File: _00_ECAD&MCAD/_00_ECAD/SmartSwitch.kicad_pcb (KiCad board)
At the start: 2 copper layers, 87 x 63 mm, 61 parts, among them J1 SWITCH, K1 G5LE-1, K2 G5LE-1, Q1 MMBT5550L, Q2 MMBT5550L, Q3 MMBT5550L, Q4 MMBT5550L, U1 DS1822, U2 ESP-12F, U3 MCP1825S

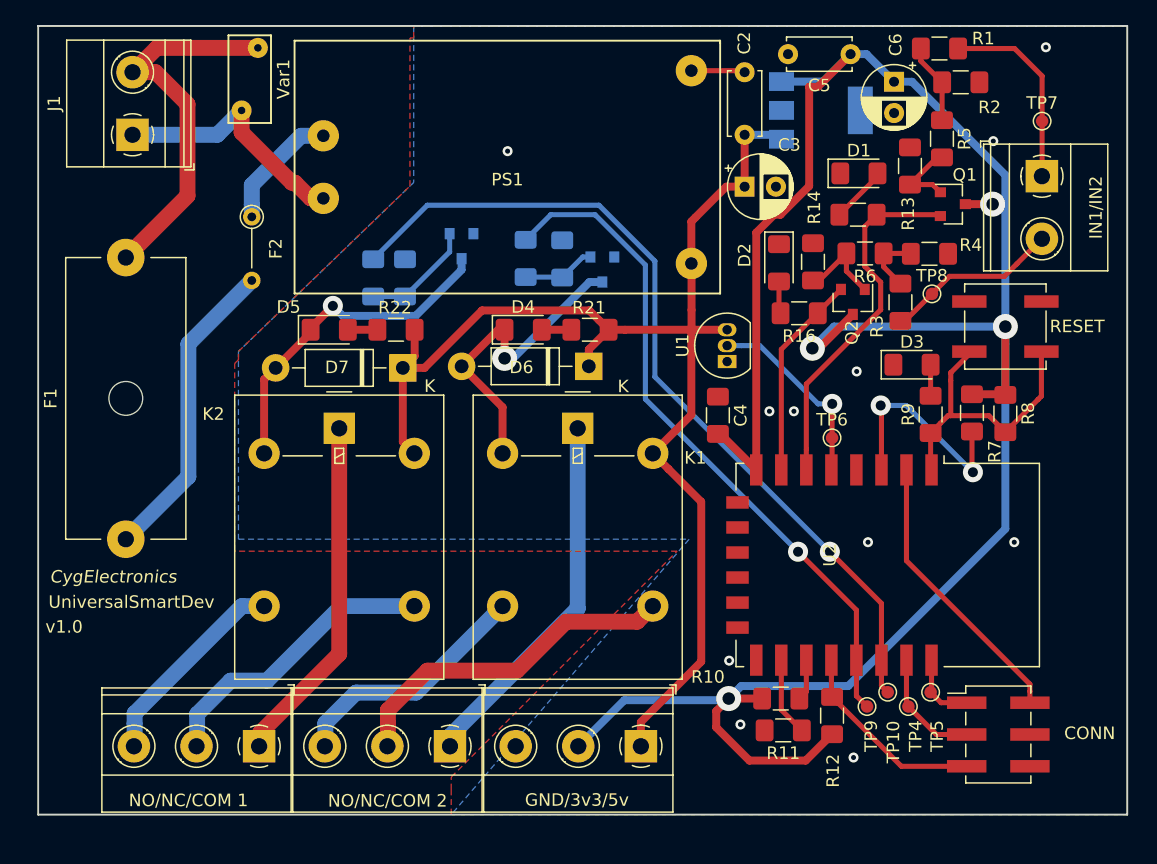
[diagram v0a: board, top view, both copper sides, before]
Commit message: Fix LED, common emitter issue, add adc feature
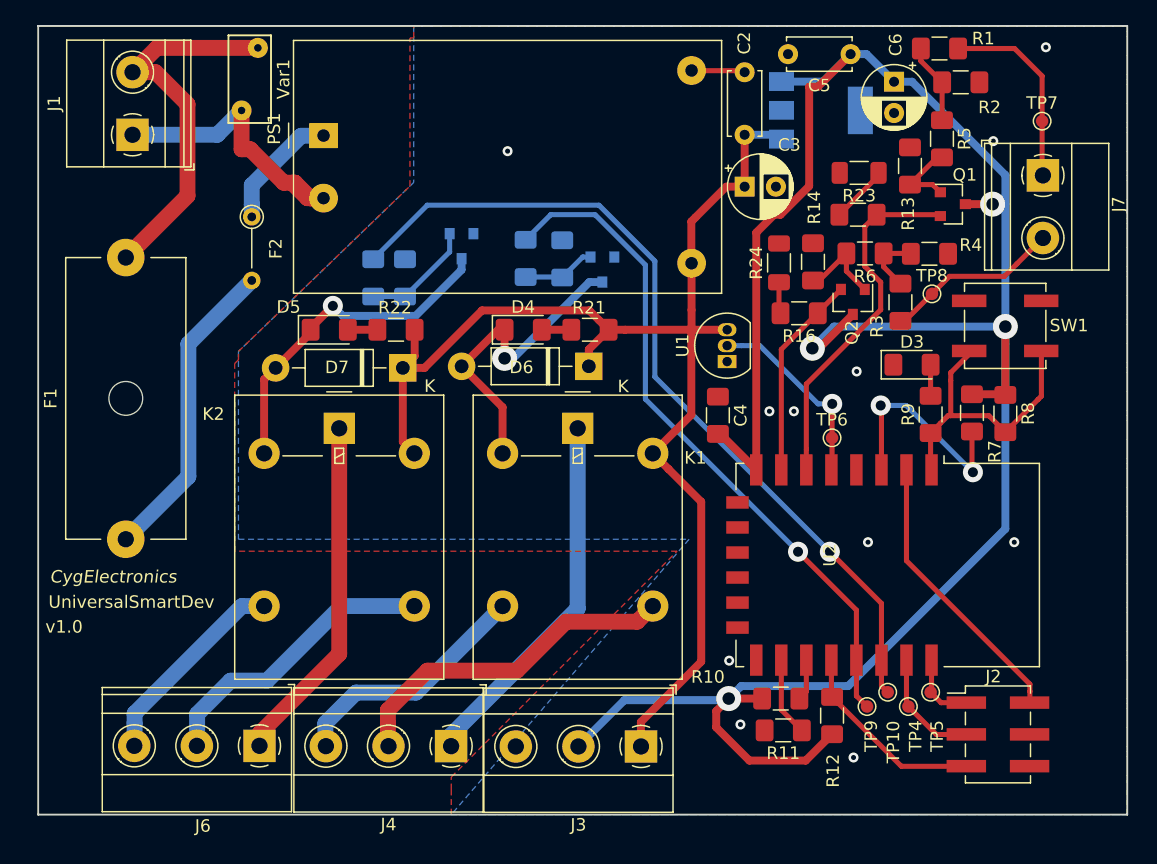
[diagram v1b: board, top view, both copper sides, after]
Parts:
- removed CONN: Conn_02x03_Counter_Clockwise, Connector_PinHeader_2.54mm:PinHeader_2x03_P2.54mm_Vertical_SMD
- removed D1, D2: LED, LED_SMD:LED_1206_3216Metric_Pad1.42x1.75mm_HandSolder
- removed GND/3v3/5v: Screw_Terminal_01x03, TerminalBlock_Phoenix:TerminalBlock_Phoenix_MKDS-1,5-3_1x03_P5.00mm_Horizontal
- removed IN1/IN2: INPUT, TerminalBlock_Phoenix:TerminalBlock_Phoenix_MKDS-1,5-2_1x02_P5.00mm_Horizontal
- removed NO/NC/COM 1: Screw_Terminal_01x03, TerminalBlock_Phoenix:TerminalBlock_Phoenix_MKDS-1,5-3_1x03_P5.00mm_Horizontal
- removed NO/NC/COM 2: Screw_Terminal_01x03, TerminalBlock_Phoenix:TerminalBlock_Phoenix_MKDS-1,5-3_1x03_P5.00mm_Horizontal
- removed RESET: RESET, Button_Switch_SMD:SW_SPST_B3SL-1022P
- added J2: Conn_02x03_Counter_Clockwise, Connector_PinHeader_2.54mm:PinHeader_2x03_P2.54mm_Vertical_SMD, F.Cu at (171.7, 141.6)
- added J3: Screw_Terminal_01x03, TerminalBlock_Phoenix:TerminalBlock_Phoenix_MKDS-1,5-3_1x03_P5.00mm_Horizontal, F.Cu at (143.2, 142.6)
- added J4: Screw_Terminal_01x03, TerminalBlock_Phoenix:TerminalBlock_Phoenix_MKDS-1,5-3_1x03_P5.00mm_Horizontal, F.Cu at (128.0, 142.5)
- added J6: Screw_Terminal_01x03, TerminalBlock_Phoenix:TerminalBlock_Phoenix_MKDS-1,5-3_1x03_P5.00mm_Horizontal, F.Cu at (112.7, 142.5)
- added J7: INPUT, TerminalBlock_Phoenix:TerminalBlock_Phoenix_MKDS-1,5-2_1x02_P5.00mm_Horizontal, F.Cu at (175.3, 96.9)
- added R23: 10k, Resistor_SMD:R_1206_3216Metric_Pad1.30x1.75mm_HandSolder, F.Cu at (160.6, 96.7)
- added R24: 10k, Resistor_SMD:R_1206_3216Metric_Pad1.30x1.75mm_HandSolder, F.Cu at (154.2, 103.9)
- added SW1: RESET, Button_Switch_SMD:SW_SPST_B3SL-1022P, F.Cu at (172.3, 109.0)
- PS1: footprint Our:HLK-PM01 -> Converter_ACDC:Converter_ACDC_HiLink_HLK-PMxx
- moved PS1 14.9 mm to (117.8, 93.8)
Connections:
- U2 pad 10: Net-(U2-Pad10) -> unconnected-(U2-Pad10)
- U2 pad 11: Net-(U2-Pad11) -> unconnected-(U2-Pad11)
- U2 pad 12: Net-(U2-Pad12) -> unconnected-(U2-Pad12)
- U2 pad 13: Net-(U2-Pad13) -> unconnected-(U2-Pad13)
- U2 pad 14: Net-(U2-Pad14) -> unconnected-(U2-Pad14)
- U2 pad 4: Net-(U2-Pad4) -> unconnected-(U2-Pad4)
- U2 pad 9: Net-(U2-Pad9) -> unconnected-(U2-Pad9)
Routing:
- net N: track 20.0 -> 24.1 mm
